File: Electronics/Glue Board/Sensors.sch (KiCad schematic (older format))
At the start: 1 part, among them U4 ADS1115IDGS

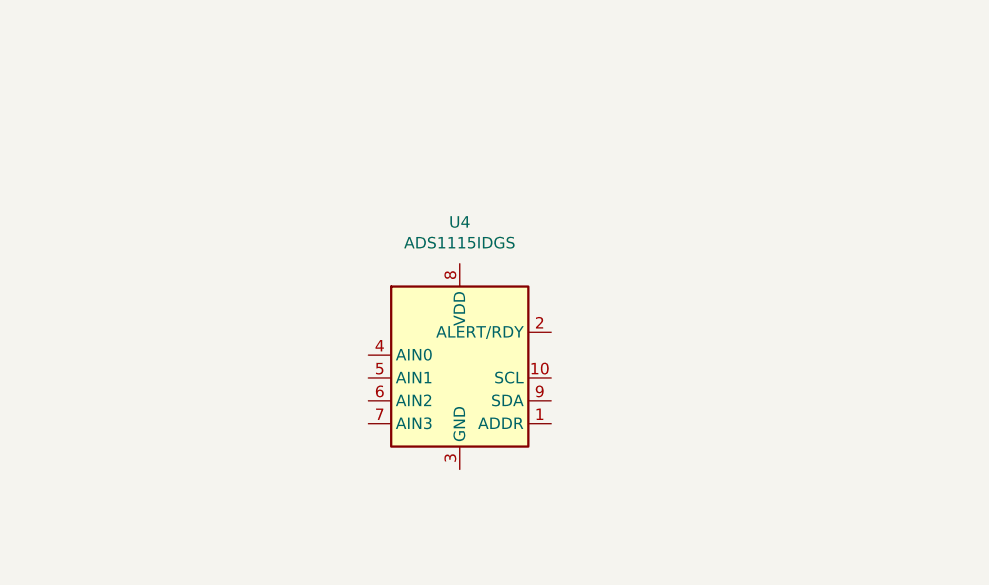
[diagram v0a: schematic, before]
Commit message: Finished the schematic for the most parts
Finished the schematic for the most parts
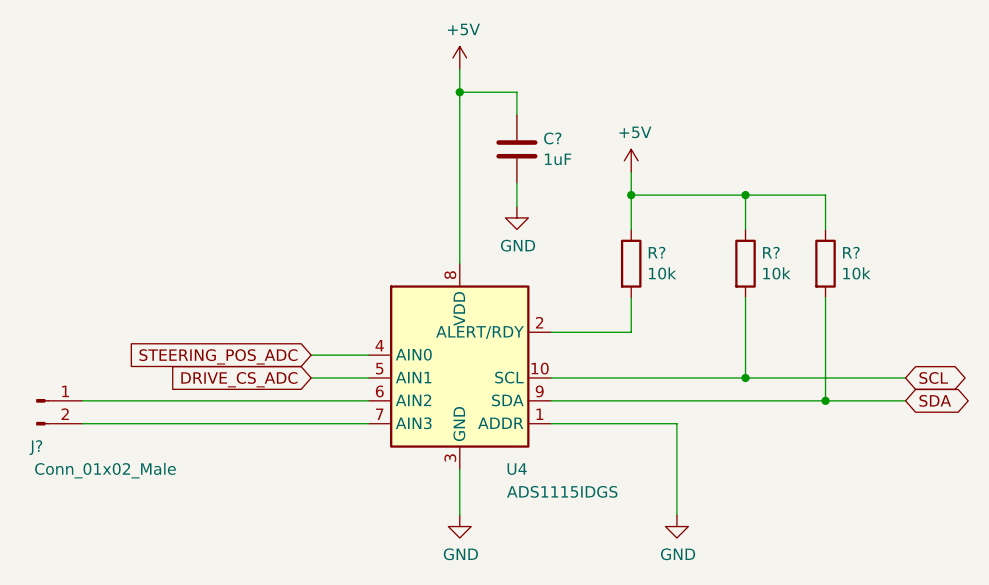
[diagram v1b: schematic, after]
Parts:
- added C?: 1uF, symbol Device:C
- added J?: Conn_01x02_Male, symbol Connector:Conn_01x02_Male
- added R? (x3): 10k, symbol Device:R
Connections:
- net GND: now reaches U4.1 (ADDR)
- net GND: now also U4.3 (GND), C?.2
- net SCL: now reaches U4.10 (SCL)
- net SCL: now also R?.2
- net at U4.2 (ALERT/RDY): now also R?.2
- net STEERING_POS_ADC: now reaches U4.4 (AIN0)
- net DRIVE_CS_ADC: now reaches U4.5 (AIN1)
- net at U4.6 (AIN2): now also J?.1 (Pin_1)
- net at U4.7 (AIN3): now also J?.2 (Pin_2)
- net +5V: now reaches U4.8 (VDD)
- net +5V: now also C?.1, R?.1, R?.1, R?.1
- net SDA: now reaches U4.9 (SDA)
- net SDA: now also R?.2
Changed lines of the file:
@@
 AR Path="/5E067AB7" Ref="U?"  Part="1"
 AR Path="/5E058596/5E067AB7" Ref="U4"  Part="1"
-F 0 "U4" H 4050 3081 50  0000 C CNN
-F 1 "ADS1115IDGS" H 4050 2990 50  0000 C CNN
+F 0 "U4" H 4300 2000 50  0000 C CNN
+F 1 "ADS1115IDGS" H 4500 1900 50  0000 C CNN
 F 2 "Package_SO:TSSOP-10_3x3mm_P0.5mm" H 4050 1900 50  0001 C CNN
 F 3 "http://www.ti.com/lit/ds/symlink/ads1113.pdf" H 4000 1500 50  0001 C CNN
@@
 	1    0    0    -1
 $EndComp
+$Comp
+L power:GND #PWR?
+U 1 1 5E314BBD
+P 4050 3000
+F 0 "#PWR?" H 4050 2750 50  0001 C CNN
+F 1 "GND" H 4055 2827 50  0000 C CNN
+F 2 "" H 4050 3000 50  0001 C CNN
+F 3 "" H 4050 3000 50  0001 C CNN
+	1    4050 3000
+	1    0    0    -1
+$EndComp
+$Comp
+L power:+5V #PWR?
+U 1 1 5E3152F6
+P 4050 1050
+F 0 "#PWR?" H 4050 900 50  0001 C CNN
+F 1 "+5V" H 4065 1223 50  0000 C CNN
+F 2 "" H 4050 1050 50  0001 C CNN
+F 3 "" H 4050 1050 50  0001 C CNN
+	1    4050 1050
+	1    0    0    -1
+$EndComp
+$Comp
+L power:GND #PWR?
+U 1 1 5E3159BD
+P 5000 3000
+F 0 "#PWR?" H 5000 2750 50  0001 C CNN
+F 1 "GND" H 5005 2827 50  0000 C CNN
+F 2 "" H 5000 3000 50  0001 C CNN
+F 3 "" H 5000 3000 50  0001 C CNN
+	1    5000 3000
+	1    0    0    -1
+$EndComp
+Wire Wire Line
+	4450 2600 5000 2600
+Wire Wire Line
+	5000 2600 5000 3000
+Wire Wire Line
+	4050 2800 4050 3000
+$Comp
+L Device:R R?
+U 1 1 5E3160E6
+P 4800 1900
+F 0 "R?" H 4870 1946 50  0000 L CNN
+F 1 "10k" H 4870 1855 50  0000 L CNN
+F 2 "" V 4730 1900 50  0001 C CNN
+F 3 "~" H 4800 1900 50  0001 C CNN
+	1    4800 1900
+	1    0    0    -1
+$EndComp
+$Comp
+L Device:R R?
+U 1 1 5E31690D
+P 5300 1900
+F 0 "R?" H 5370 1946 50  0000 L CNN
+F 1 "10k" H 5370 1855 50  0000 L CNN
+F 2 "" V 5230 1900 50  0001 C CNN
+F 3 "~" H 5300 1900 50  0001 C CNN
+	1    5300 1900
+	1    0    0    -1
+$EndComp
+$Comp
+L Device:R R?
+U 1 1 5E316F25
+P 5650 1900
+F 0 "R?" H 5720 1946 50  0000 L CNN
+F 1 "10k" H 5720 1855 50  0000 L CNN
+F 2 "" V 5580 1900 50  0001 C CNN
+F 3 "~" H 5650 1900 50  0001 C CNN
+	1    5650 1900
+	1    0    0    -1
+$EndComp
+$Comp
+L power:+5V #PWR?
+U 1 1 5E317505
+P 4800 1500
+F 0 "#PWR?" H 4800 1350 50  0001 C CNN
+F 1 "+5V" H 4815 1673 50  0000 C CNN
+F 2 "" H 4800 1500 50  0001 C CNN
+F 3 "" H 4800 1500 50  0001 C CNN
+	1    4800 1500
+	1    0    0    -1
+$EndComp
+Wire Wire Line
+	4450 2200 4800 2200
+Wire Wire Line
+	4800 2200 4800 2050
+Wire Wire Line
+	4450 2400 5300 2400
+Wire Wire Line
+	5300 2400 5300 2050
+Wire Wire Line
+	4450 2500 5650 2500
+Wire Wire Line
+	5650 2500 5650 2050
+Wire Wire Line
+	5300 1750 5300 1600
+Wire Wire Line
+	5300 1600 4800 1600
+Wire Wire Line
+	4800 1600 4800 1750
+Wire Wire Line
+	5300 1600 5650 1600
+Wire Wire Line
+	5650 1600 5650 1750
+Connection ~ 5300 1600
+Wire Wire Line
+	4800 1500 4800 1600
+Connection ~ 4800 1600
+Text GLabel 6000 2400 2    50   BiDi ~ 0
+SCL
+Text GLabel 6000 2500 2    50   BiDi ~ 0
+SDA
+Wire Wire Line
+	5300 2400 6000 2400
+Connection ~ 5300 2400
+Wire Wire Line
+	6000 2500 5650 2500
+Connection ~ 5650 2500
+Text GLabel 3400 2400 0    50   Input ~ 0
+DRIVE_CS_ADC
+$Comp
+L Device:C C?
+U 1 1 5E31A1E4
+P 4300 1400
+F 0 "C?" H 4415 1446 50  0000 L CNN
+F 1 "1uF" H 4415 1355 50  0000 L CNN
+F 2 "" H 4338 1250 50  0001 C CNN
+F 3 "~" H 4300 1400 50  0001 C CNN
+	1    4300 1400
+	1    0    0    -1
+$EndComp
+$Comp
+L power:GND #PWR?
+U 1 1 5E31B40D
+P 4300 1650
+F 0 "#PWR?" H 4300 1400 50  0001 C CNN
+F 1 "GND" H 4305 1477 50  0000 C CNN
+F 2 "" H 4300 1650 50  0001 C CNN
+F 3 "" H 4300 1650 50  0001 C CNN
+	1    4300 1650
+	1    0    0    -1
+$EndComp
+Wire Wire Line
+	4300 1550 4300 1650
+Wire Wire Line
+	4300 1250 4300 1150
+Wire Wire Line
+	4300 1150 4050 1150
+Wire Wire Line
+	4050 1150 4050 1900
+Wire Wire Line
+	4050 1050 4050 1150
+Connection ~ 4050 1150
+$Comp
+L Connector:Conn_01x02_Male J?
+U 1 1 5E31D258
+P 2200 2500
+F 0 "J?" H 2200 2300 50  0000 C CNN
+F 1 "Conn_01x02_Male" H 2500 2200 50  0000 C CNN
+F 2 "" H 2200 2500 50  0001 C CNN
+F 3 "~" H 2200 2500 50  0001 C CNN
+	1    2200 2500
+	1    0    0    -1
+$EndComp
+Wire Wire Line
+	2400 2500 3650 2500
+Wire Wire Line
+	3650 2600 2400 2600
+Wire Wire Line
+	3400 2300 3650 2300
+Wire Wire Line
+	3650 2400 3400 2400
+Text GLabel 3400 2300 0    50   Input ~ 0
+STEERING_POS_ADC
 $EndSCHEMATC

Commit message: Complete Schematic and BOM
Complete Schematic and BOM. Next up, layout!
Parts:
- removed J?: Conn_01x02_Male, symbol Connector:Conn_01x02_Male
- added J7: Conn_01x04_Female, Connector_PinHeader_2.54mm:PinHeader_1x04_P2.54mm_Vertical, symbol Connector:Conn_01x04_Female
- C17: renamed from C?; footprint (none) -> Capacitor_SMD:C_0805_2012Metric; MPN (none) -> C0805C105K4RACTU
- R31, R32, R33: renamed from R?; footprint (none) -> Resistor_SMD:R_0603_1608Metric; MPN (none) -> RC0603FR-0710KL
- U4: MPN (none) -> ADS1115IDGSR
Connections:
- net GND: now also J7.1 (Pin_1), J7.3 (Pin_3)
- net at U4.6 (AIN2): now also J7.4 (Pin_4)
- net at U4.7 (AIN3): now also J7.2 (Pin_2)
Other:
- note added: "I2C ADDRESS: 1001_000X (0x90)"
- note added: "SPARE\nADC\nINPUTS"
- moved on the sheet: C17, R31, R32, R33, U4

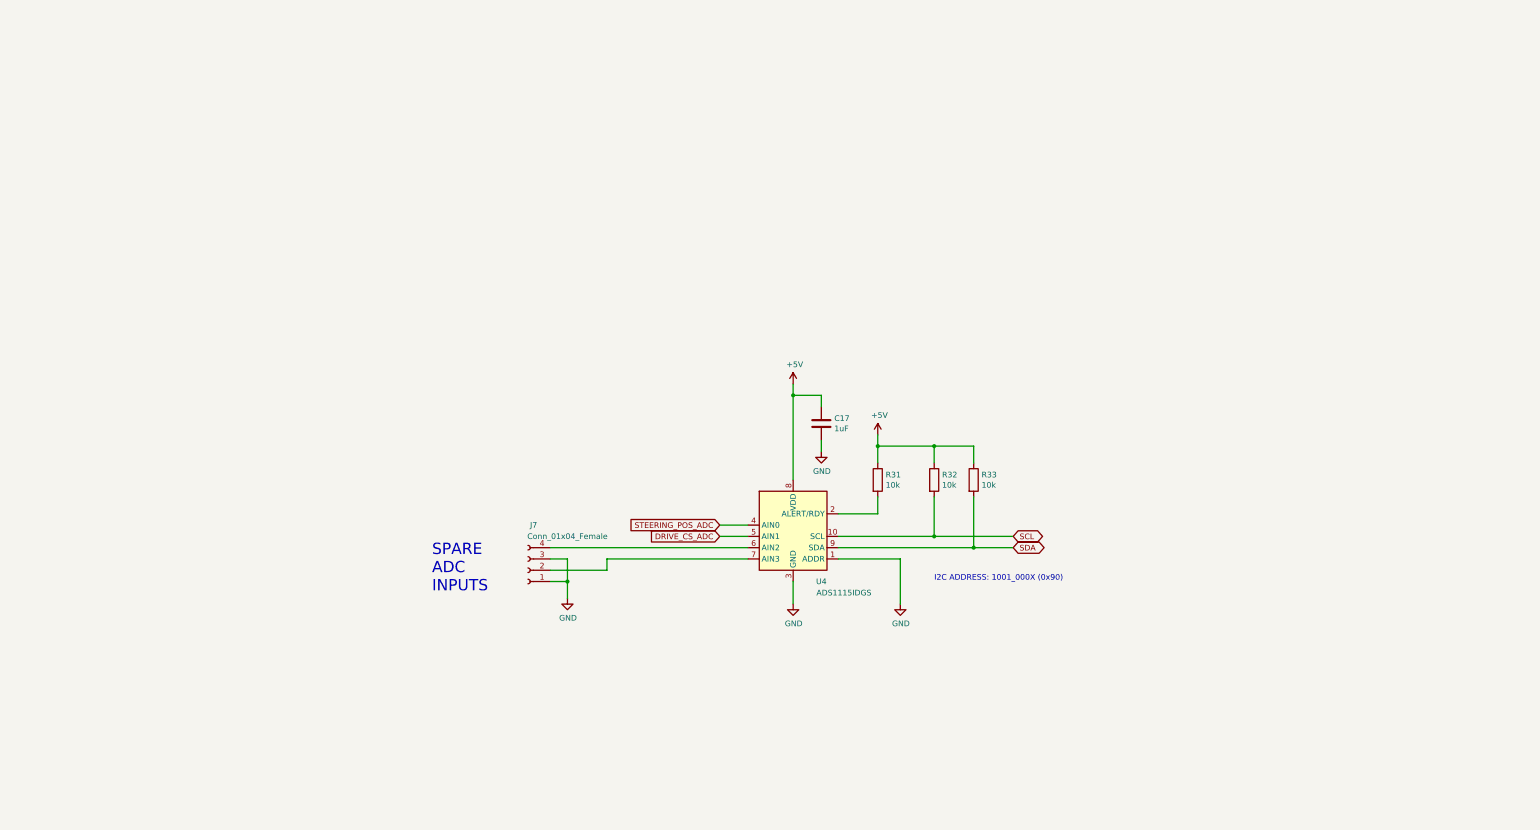
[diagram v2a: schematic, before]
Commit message: Added Motor v-sense and battery mon. Layout time!
Added Motor v-sense and battery mon. Layout time!
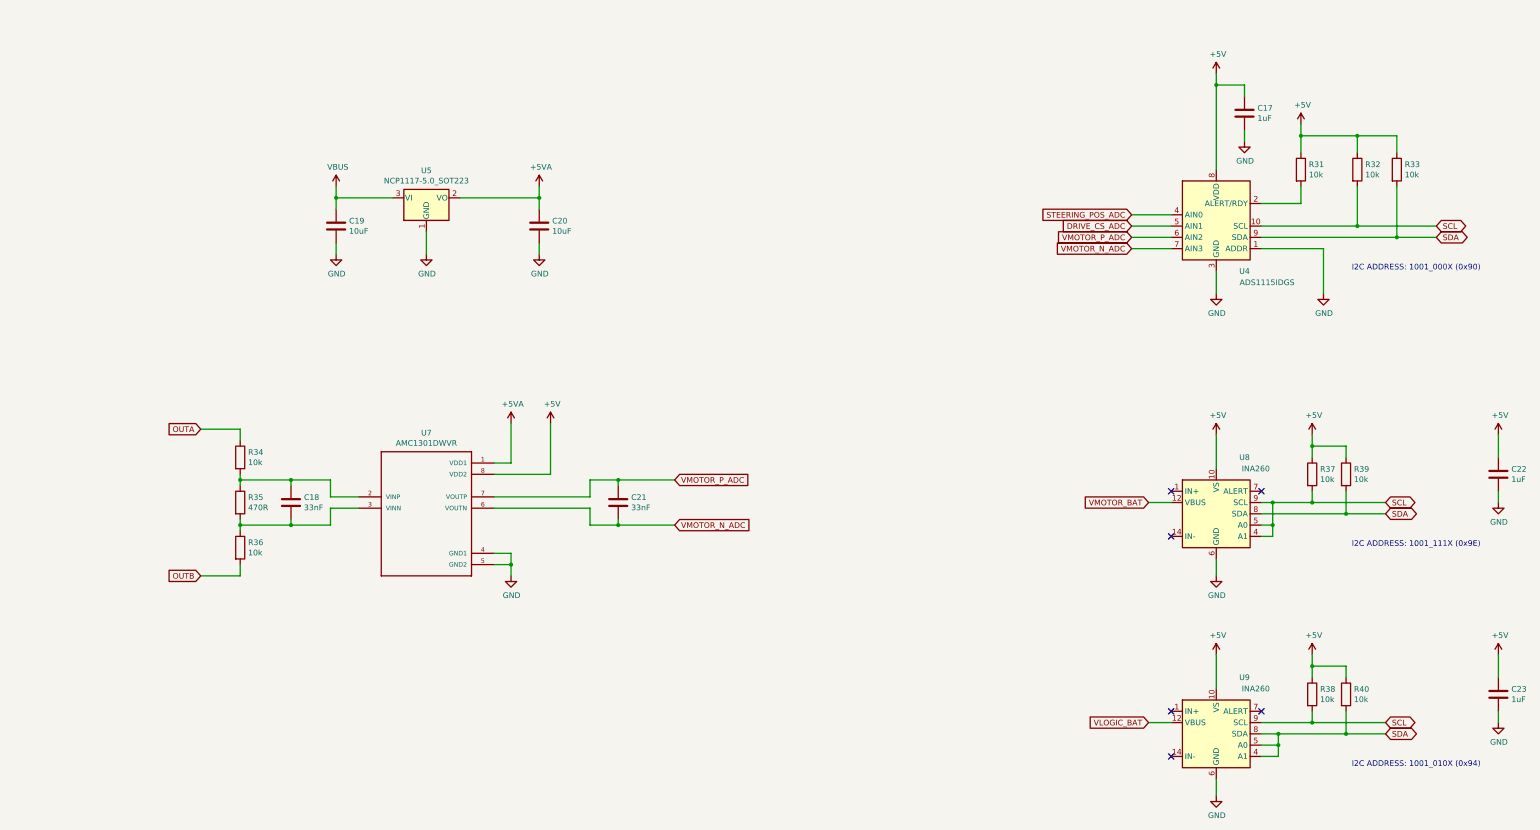
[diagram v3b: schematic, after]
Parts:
- removed J7: Conn_01x04_Female, Connector_PinHeader_2.54mm:PinHeader_1x04_P2.54mm_Vertical, symbol Connector:Conn_01x04_Female
- added C18, C21: 33nF, Capacitor_SMD:C_0805_2012Metric, symbol Device:C
- added C19, C20: 10uF, Capacitor_SMD:C_0805_2012Metric, symbol Device:C
- added C22, C23: 1uF, Capacitor_SMD:C_0805_2012Metric, symbol Device:C
- added R34, R36, R37, R38, R39, R40: 10k, Resistor_SMD:R_0603_1608Metric, symbol Device:R
- added R35: 470R, Resistor_SMD:R_0603_1608Metric, symbol Device:R
- added U5: NCP1117-5.0_SOT223, Package_TO_SOT_SMD:SOT-223-3_TabPin2, symbol Regulator_Linear:NCP1117-5.0_SOT223
- added U7: AMC1301DWVR, libs:SOIC127P1150X280-8N, symbol AMC1301DWVR:AMC1301DWVR
- added U8, U9: INA260, Package_SO:TSSOP-16_4.4x5mm_P0.65mm, symbol Sensor:INA260
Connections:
- net +5V: now also C22.1, C23.1, R37.1, R38.1, R39.1, R40.1, U7.8 (VDD2), U8.10 (VS), U9.10 (VS)
- net GND: now also C19.2, C20.2, C22.2, C23.2, U5.1 (GND), U7.4 (GND1), U7.5 (GND2), U8.11 (GND), U8.6 (GND), U9.11 (GND), U9.6 (GND)
- net SCL: now also R37.2, R38.2, U8.4 (A1), U8.5 (A0), U8.9 (SCL), U9.9 (SCL)
- net SDA: now also R39.2, R40.2, U8.8 (SDA), U9.4 (A1), U9.5 (A0), U9.8 (SDA)
- net VMOTOR_P_ADC: now reaches U4.6 (AIN2)
- net VMOTOR_P_ADC: now also C21.1, U7.7 (VOUTP)
- net VMOTOR_N_ADC: now reaches U4.7 (AIN3)
- net VMOTOR_N_ADC: now also C21.2, U7.6 (VOUTN)
- new net: C18.1, R34.2, R35.1, U7.2 (VINP)
- new net: C18.2, R35.2, R36.1, U7.3 (VINN)
- new net: U8.1 (IN+), U8.2 (IN+), U8.3 (IN+)
- new net: U8.14 (IN-), U8.15 (IN-), U8.16 (IN-)
- new net: U9.1 (IN+), U9.2 (IN+), U9.3 (IN+)
- new net: U9.14 (IN-), U9.15 (IN-), U9.16 (IN-)
- new net +5VA: C20.1, U5.2 (VO), U7.1 (VDD1)
- new net OUTA: R34.1
- new net OUTB: R36.2
- new net VBUS: C19.1, U5.3 (VI)
- new net VLOGIC_BAT: U9.12 (VBUS)
- new net VMOTOR_BAT: U8.12 (VBUS)
- no-connect marks 0 -> 6
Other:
- note added: "I2C ADDRESS: 1001_010X (0x94)"
- note added: "I2C ADDRESS: 1001_111X (0x9E)"
- note removed: "SPARE\nADC\nINPUTS"
- moved on the sheet: C17, R31, R32, R33, U4

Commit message: Updated Readme
Updated Readme
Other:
- note added: "ADC - ADS1115IDGS\n\nI2C ADDRESS: 1001_000X (0x90)\nSHIFTED ADY: 0100_1000 (0x48)"
- note added: "VLOGIC BATTERY SENSE - INA260\n\nI2C ADDRESS: 1001_010X (0x94)\nSHIFTED ADY: 0100_1010 (0x4A)"
- note added: "VMOTOR BATTERY SENSE - INA260\n\nI2C ADDRESS: 1001_111X (0x9E)\nSHIFTED ADY: 0100_1111 (0x4F)"
- note removed: "I2C ADDRESS: 1001_000X (0x90)"
- note removed: "I2C ADDRESS: 1001_010X (0x94)"
- note removed: "I2C ADDRESS: 1001_111X (0x9E)"
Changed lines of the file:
@@
 Text GLabel 11250 2650 0    50   Input ~ 0
 STEERING_POS_ADC
-Text Notes 13200 3150 0    50   ~ 0
-I2C ADDRESS: 1001_000X (0x90)
+Text Notes 13200 3350 0    50   ~ 0
+ADC - ADS1115IDGS\n\nI2C ADDRESS: 1001_000X (0x90)\nSHIFTED ADY: 0100_1000  (0x48)
 Text GLabel 3000 4550 0    50   Input ~ 0
 OUTA
@@
 Wire Wire Line
 	12500 5200 12850 5200
-Text Notes 13200 5600 0    50   ~ 0
-I2C ADDRESS: 1001_111X (0x9E)
+Text Notes 13200 5800 0    50   ~ 0
+VMOTOR BATTERY SENSE - INA260\n\nI2C ADDRESS: 1001_111X (0x9E)\nSHIFTED ADY: 0100_1111  (0x4F)
 Wire Wire Line
 	12400 5300 13150 5300
@@
 	12550 7450 12550 7350
 Connection ~ 12550 7350
-Text Notes 13200 7550 0    50   ~ 0
-I2C ADDRESS: 1001_010X (0x94)
+Text Notes 13200 7800 0    50   ~ 0
+VLOGIC BATTERY SENSE - INA260\n\nI2C ADDRESS: 1001_010X (0x94)\nSHIFTED ADY: 0100_1010  (0x4A)
 $Comp
 L Device:C C23

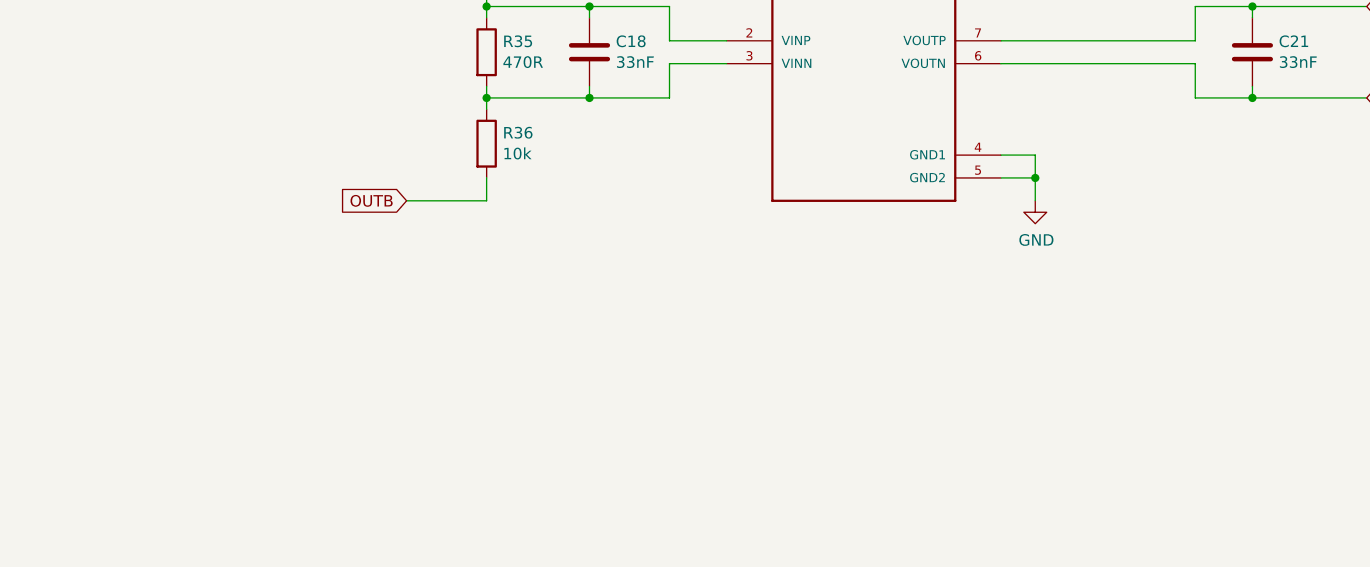
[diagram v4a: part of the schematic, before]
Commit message: Added schematic change notes for REV B
Added schematic change notes for REV B
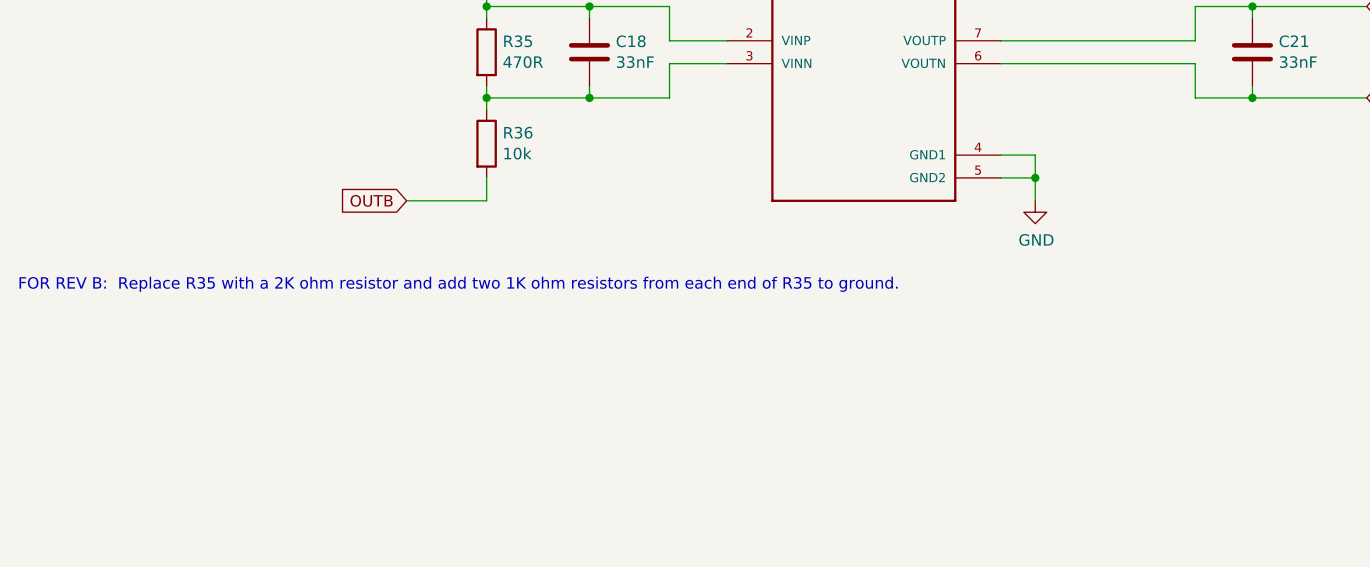
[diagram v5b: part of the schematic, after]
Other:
- note added: "FOR REV B: Replace R35 with a 2K ohm resistor and add two 1K ohm resistors from each end of R35 to ground."
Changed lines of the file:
@@
 Wire Wire Line
 	14500 7050 14500 7150
+Text Notes 1300 6250 0    50   ~ 0
+FOR REV B:  Replace R35 with a 2K ohm resistor and add two 1K ohm resistors from each end of R35 to ground.
 $EndSCHEMATC
